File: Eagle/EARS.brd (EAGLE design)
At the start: 30.7 x 44.5 mm, 32 parts, among them IC1 LM386MM-1, J1 1X2-3.5MM, J2 CORTEX_DEBUG_SMD, Q1 IRLb8721, X1 ECX_34G

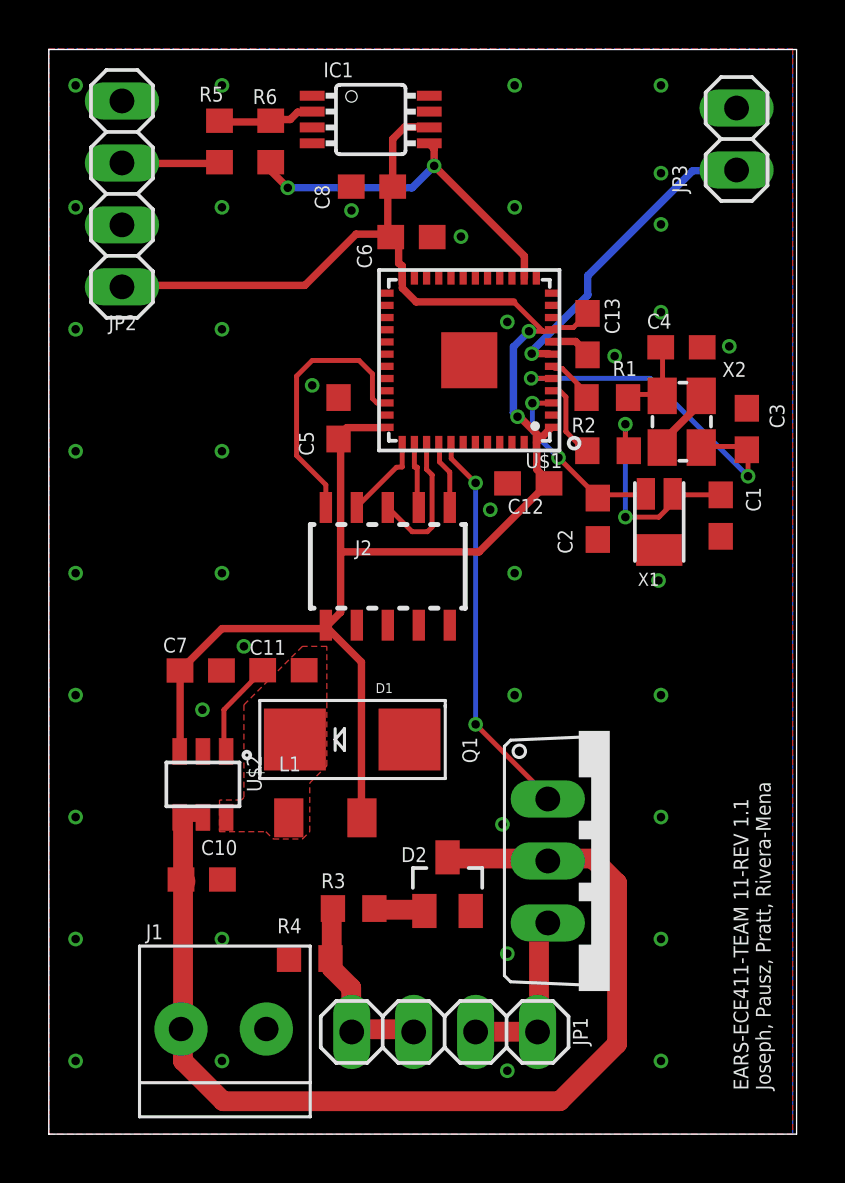
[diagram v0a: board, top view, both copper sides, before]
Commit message: Fixed Silk Screen
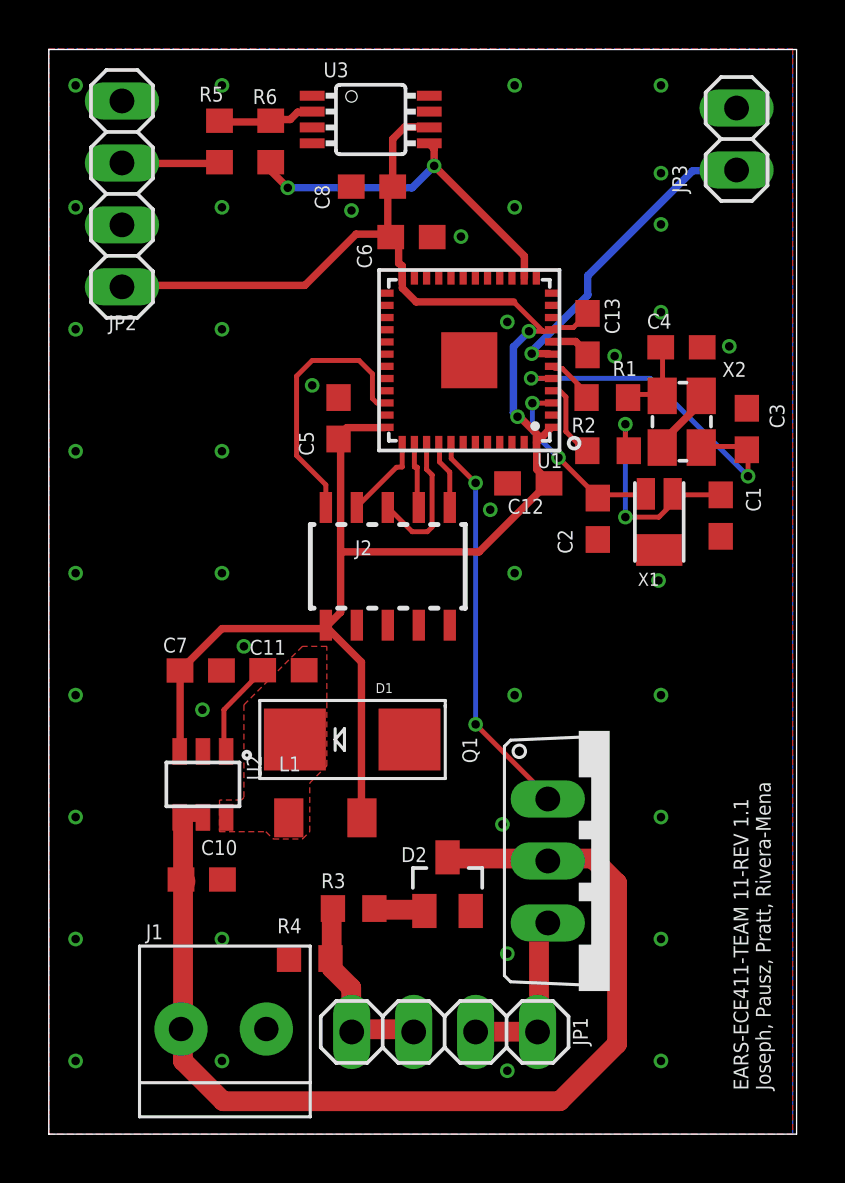
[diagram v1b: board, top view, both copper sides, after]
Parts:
- renumbered IC1 to U3, U$1 to U1, U$2 to U2
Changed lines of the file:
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@@
 <attribute name="SPICEPREFIX" value="R" x="-17.71" y="66.12" size="1.778" layer="27" rot="R180" display="off"/>
 </element>
-<element name="U$1" library="EARS" package="UFQFPN48" value="STM32LXX" x="17.24" y="31.73" smashed="yes" rot="R180">
+<element name="U1" library="EARS" package="UFQFPN48" value="STM32LXX" x="17.24" y="31.73" smashed="yes" rot="R180">
 <attribute name="NAME" x="21.05" y="27.92" size="0.6096" layer="25" rot="R180"/>
 <attribute name="VALUE" x="21.05" y="36.41" size="0.6096" layer="27" rot="R180"/>
 </element>
-<element name="U$2" library="EARS" package="TI_SOT6" value="LMR160067Q3" x="6.32" y="14.34" smashed="yes" rot="R270">
+<element name="U2" library="EARS" package="TI_SOT6" value="LMR160067Q3" x="6.32" y="14.34" smashed="yes" rot="R270">
 <attribute name="NAME" x="8.12" y="15.54" size="0.6096" layer="25" rot="R270"/>
 </element>
@@
 <attribute name="SPICEPREFIX" value="R" x="10.7" y="7.2" size="0.6096" layer="27" rot="R180" display="off"/>
 </element>
-<element name="IC1" library="linear" library_urn="urn:adsk.eagle:library:262" package="MMSOP08" package3d_urn="urn:adsk.eagle:package:16476/2" value="LM386MM-1" x="13.2" y="41.6" smashed="yes" rot="R270">
+<element name="U3" library="linear" library_urn="urn:adsk.eagle:library:262" package="MMSOP08" package3d_urn="urn:adsk.eagle:package:16476/2" value="LM386MM-1" x="13.2" y="41.6" smashed="yes" rot="R270">
 <attribute name="NAME" x="11.26" y="43.332" size="0.6096" layer="25" ratio="10"/>
 </element>
@@
 <signals>
 <signal name="3V3">
-<contactref element="U$1" pad="48"/>
-<contactref element="U$1" pad="1"/>
-<contactref element="U$1" pad="9"/>
-<contactref element="U$1" pad="24"/>
-<contactref element="U$1" pad="36"/>
+<contactref element="U1" pad="48"/>
+<contactref element="U1" pad="1"/>
+<contactref element="U1" pad="9"/>
+<contactref element="U1" pad="24"/>
+<contactref element="U1" pad="36"/>
 <contactref element="C5" pad="2"/>
 <contactref element="C7" pad="2"/>
@@
 <contactref element="L1" pad="2"/>
 <contactref element="C12" pad="1"/>
-<contactref element="U$2" pad="3"/>
+<contactref element="U2" pad="3"/>
 <contactref element="J2" pad="1"/>
 <wire x1="14.3444" y1="36.4236" x2="14.3444" y2="35.7044" width="0.3048" layer="1"/>
@@
 <via x="19.2188" y="29.4156" extent="1-16" drill="0.35"/>
 <via x="19.688" y="32.9184" extent="1-16" drill="0.35"/>
-<contactref element="IC1" pad="6"/>
+<contactref element="U3" pad="6"/>
 <contactref element="JP2" pad="1"/>
 <contactref element="C8" pad="2"/>
@@
 </signal>
 <signal name="MCU_P6">
-<contactref element="U$1" pad="6"/>
+<contactref element="U1" pad="6"/>
 <contactref element="R1" pad="2"/>
 <wire x1="21.05" y1="31.3944" x2="20.7452" y2="31.3944" width="0.2032" layer="1"/>
@@
 </signal>
 <signal name="8MOX_IN">
-<contactref element="U$1" pad="5"/>
+<contactref element="U1" pad="5"/>
 <contactref element="C3" pad="2"/>
 <contactref element="X2" pad="1"/>
@@
 </signal>
 <signal name="MCU_P4">
-<contactref element="U$1" pad="4"/>
+<contactref element="U1" pad="4"/>
 <contactref element="R2" pad="2"/>
 <wire x1="20.9476" y1="30.48" x2="20.615" y2="30.48" width="0.2032" layer="1"/>
@@
 </signal>
 <signal name="OSC32_OUT">
-<contactref element="U$1" pad="3"/>
+<contactref element="U1" pad="3"/>
 <contactref element="C2" pad="2"/>
 <contactref element="X1" pad="C1"/>
@@
 <contactref element="X2" pad="2"/>
 <contactref element="X2" pad="4"/>
-<contactref element="U$1" pad="44"/>
-<contactref element="U$1" pad="47"/>
-<contactref element="U$1" pad="35"/>
-<contactref element="U$1" pad="23"/>
-<contactref element="U$1" pad="T1"/>
-<contactref element="U$1" pad="8"/>
+<contactref element="U1" pad="44"/>
+<contactref element="U1" pad="47"/>
+<contactref element="U1" pad="35"/>
+<contactref element="U1" pad="23"/>
+<contactref element="U1" pad="T1"/>
+<contactref element="U1" pad="8"/>
 <contactref element="C5" pad="1"/>
 <contactref element="C7" pad="1"/>
@@
 <contactref element="D1" pad="A"/>
 <contactref element="C12" pad="2"/>
-<contactref element="U$2" pad="2"/>
+<contactref element="U2" pad="2"/>
 <contactref element="J1" pad="1"/>
 <contactref element="J2" pad="3"/>
@@
 </polygon>
 <contactref element="R4" pad="2"/>
-<contactref element="IC1" pad="4"/>
-<contactref element="IC1" pad="3"/>
+<contactref element="U3" pad="4"/>
+<contactref element="U3" pad="3"/>
 <contactref element="JP2" pad="4"/>
 <contactref element="JP2" pad="2"/>
@@
 </signal>
 <signal name="12V">
-<contactref element="U$2" pad="5"/>
-<contactref element="U$2" pad="4"/>
+<contactref element="U2" pad="5"/>
+<contactref element="U2" pad="4"/>
 <contactref element="C10" pad="2"/>
 <contactref element="J1" pad="2"/>
@@
 <contactref element="L1" pad="1"/>
 <contactref element="C11" pad="2"/>
-<contactref element="U$2" pad="6"/>
+<contactref element="U2" pad="6"/>
 <wire x1="7.334" y1="13.1064" x2="7.27" y2="12.99" width="0.1524" layer="1"/>
 <wire x1="9.7724" y1="13.1064" x2="9.84" y2="12.97" width="0.1524" layer="1"/>
@@
 </signal>
 <signal name="LMR_CB">
-<contactref element="U$2" pad="1"/>
+<contactref element="U2" pad="1"/>
 <contactref element="C11" pad="1"/>
 <wire x1="7.1816" y1="15.6972" x2="7.1816" y2="17.40065625" width="0.2032" layer="1"/>
@@
 </signal>
 <signal name="!RESET!">
-<contactref element="U$1" pad="40"/>
+<contactref element="U1" pad="40"/>
 <contactref element="J2" pad="10"/>
 <wire x1="16.0208" y1="27.5604" x2="16.0208" y2="28.3464" width="0.2032" layer="1"/>
@@
 </signal>
 <signal name="SWO">
-<contactref element="U$1" pad="39"/>
+<contactref element="U1" pad="39"/>
 <contactref element="J2" pad="6"/>
 <wire x1="15.5224" y1="24.7" x2="15.716" y2="24.8936" width="0.2032" layer="1"/>
@@
 </signal>
 <signal name="SWDIO">
-<contactref element="U$1" pad="34"/>
+<contactref element="U1" pad="34"/>
 <contactref element="J2" pad="2"/>
 <wire x1="13.87" y1="29.98" x2="13.45" y2="29.98" width="0.2032" layer="1"/>
@@
 </signal>
 <signal name="SWDCLK">
-<contactref element="U$1" pad="37"/>
+<contactref element="U1" pad="37"/>
 <contactref element="J2" pad="4"/>
 <wire x1="12.668" y1="25.7556" x2="14.253428125" y2="27.341028125" width="0.2032" layer="1"/>
@@
 </signal>
 <signal name="NC">
-<contactref element="U$1" pad="38"/>
+<contactref element="U1" pad="38"/>
 <contactref element="J2" pad="8"/>
 <wire x1="15.1064" y1="25.7556" x2="15.1064" y2="27.3464" width="0.2032" layer="1"/>
@@
 </signal>
 <signal name="NPN_DRV">
-<contactref element="U$1" pad="41"/>
+<contactref element="U1" pad="41"/>
 <contactref element="Q1" pad="1"/>
 <wire x1="16.5" y1="28.4" x2="16.5" y2="27.7" width="0.2032" layer="1"/>
@@
 </signal>
 <signal name="FB">
-<contactref element="IC1" pad="2"/>
+<contactref element="U3" pad="2"/>
 <contactref element="R5" pad="2"/>
 <contactref element="R6" pad="1"/>
@@
 <signal name="PRESSURE">
 <contactref element="R6" pad="2"/>
-<contactref element="IC1" pad="5"/>
-<contactref element="U$1" pad="14"/>
+<contactref element="U3" pad="5"/>
+<contactref element="U1" pad="14"/>
 <wire x1="9.8" y1="38.8" x2="14.9" y2="38.8" width="0.3048" layer="16"/>
 <wire x1="14.9" y1="38.8" x2="15.8" y2="39.7" width="0.3048" layer="16"/>
@@
 </signal>
 <signal name="NRST">
-<contactref element="U$1" pad="7"/>
+<contactref element="U1" pad="7"/>
 <contactref element="JP3" pad="2"/>
 <wire x1="20.5" y1="32" x2="19.8" y2="32" width="0.3048" layer="1"/>
